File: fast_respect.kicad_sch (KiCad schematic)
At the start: 16 parts, among them J1_1 Conn_02x04_Odd_Even, SW1_1 SW_Push, SW1_2 SW_Push, U1_1 STM32F446RETx

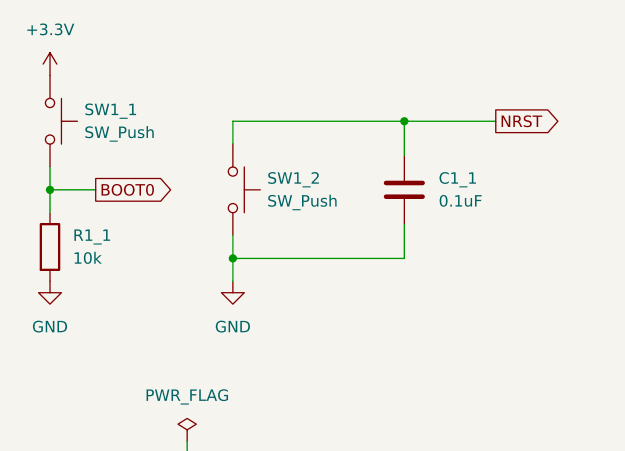
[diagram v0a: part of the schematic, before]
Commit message: 一部のスイッチの名称変更
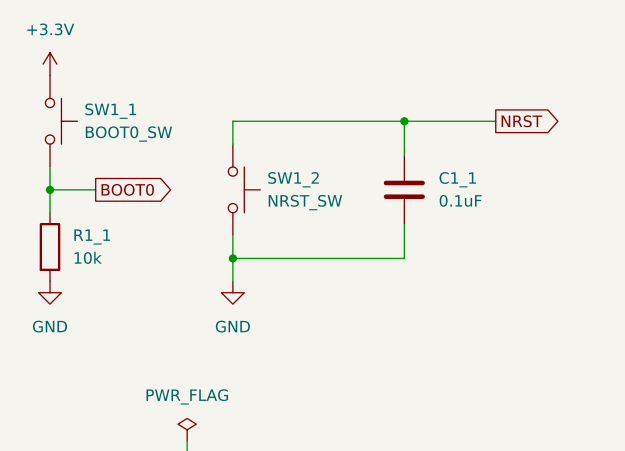
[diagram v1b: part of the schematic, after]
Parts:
- SW1_1: value SW_Push -> BOOT0_SW
- SW1_2: value SW_Push -> NRST_SW
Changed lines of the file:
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@@
       (effects (font (size 1.27 1.27)) (justify left))
     )
-    (property "Value" "SW_Push" (at 49.53 41.91 90)
+    (property "Value" "NRST_SW" (at 49.53 41.91 90)
       (effects (font (size 1.27 1.27)) (justify left))
     )
@@
       (effects (font (size 1.27 1.27)) (justify left))
     )
-    (property "Value" "SW_Push" (at 29.21 34.29 90)
+    (property "Value" "BOOT0_SW" (at 29.21 34.29 90)
       (effects (font (size 1.27 1.27)) (justify left))
     )

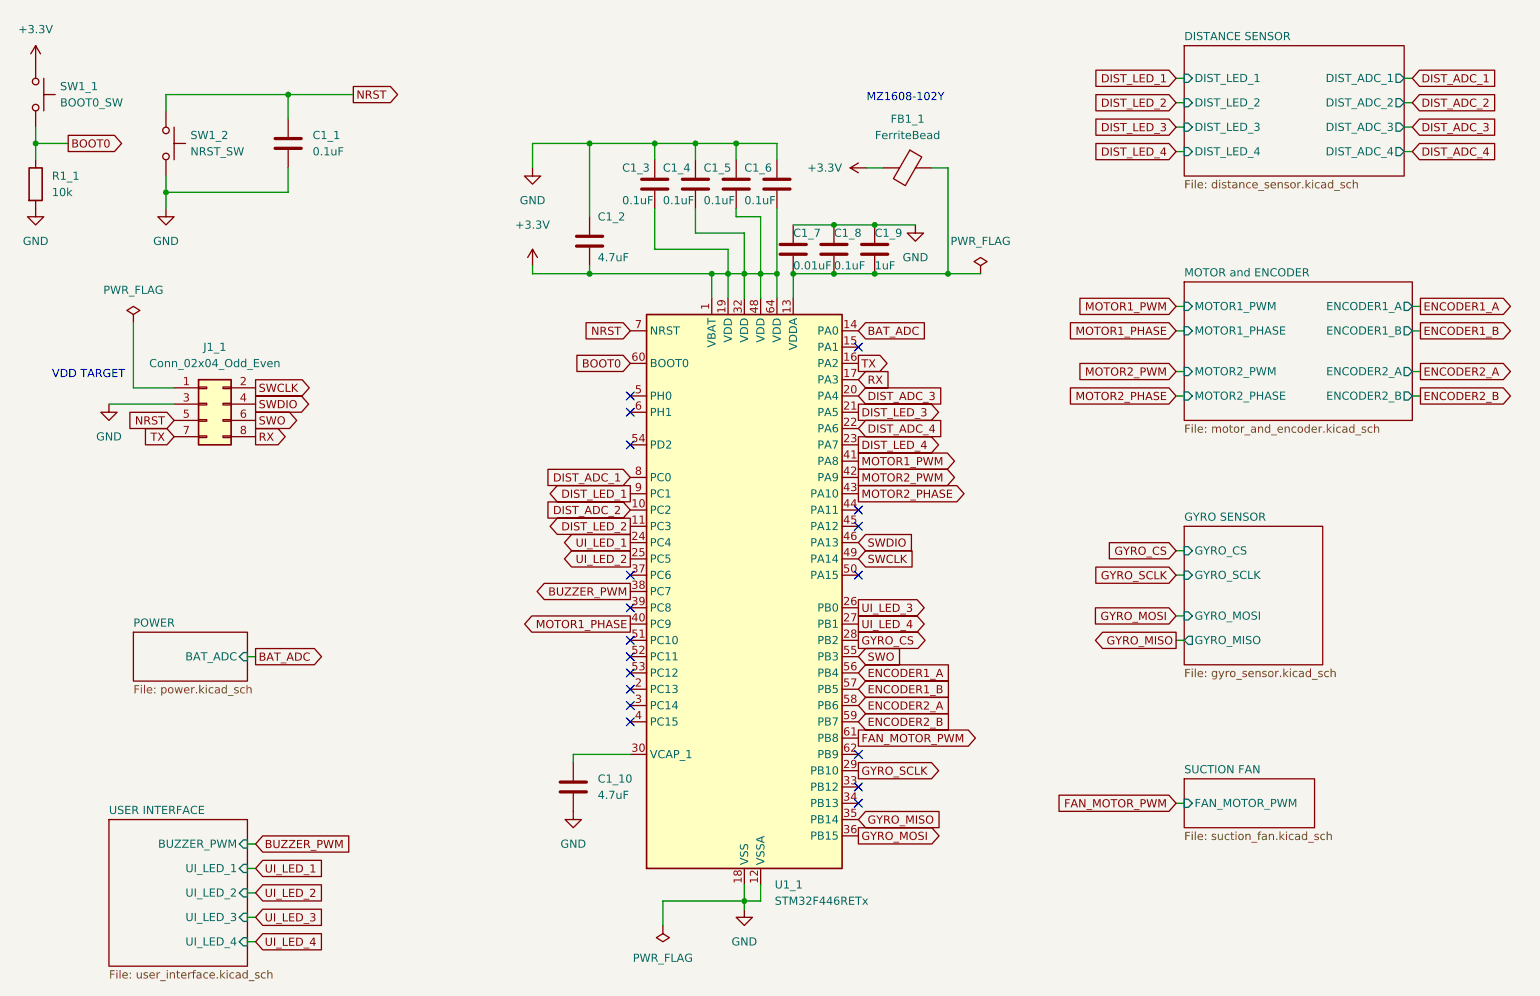
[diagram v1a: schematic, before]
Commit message: UIスイッチ３種類をマイコンピンに割り当て忘れてたので割り当てた
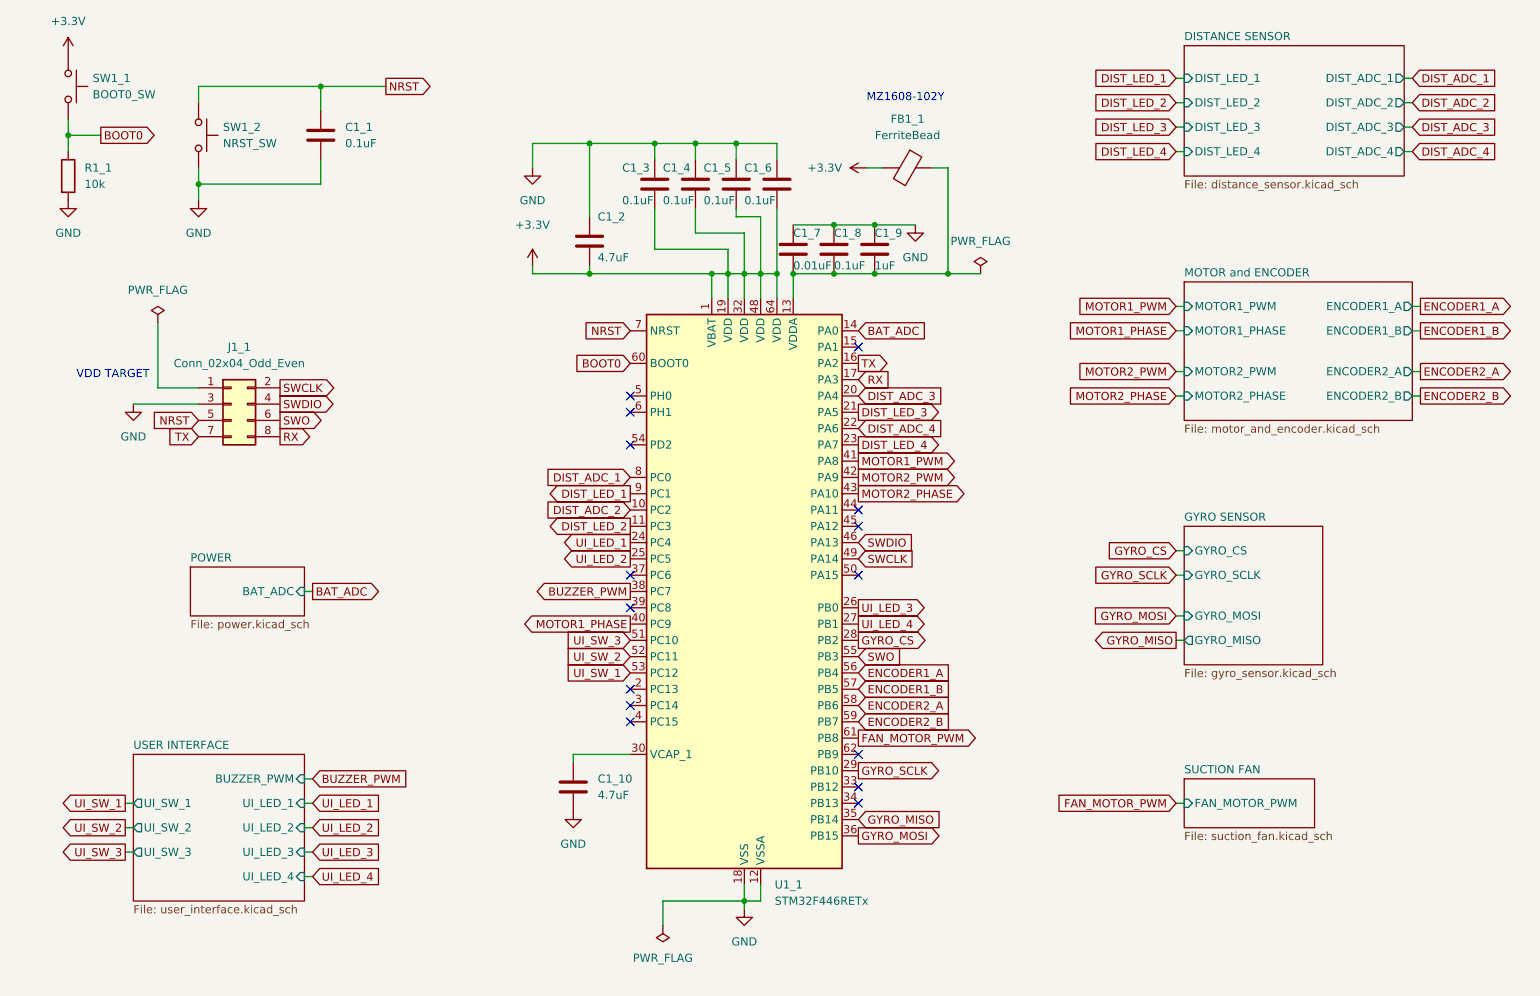
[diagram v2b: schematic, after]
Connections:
- net UI_SW_3: now reaches U1_1.51 (PC10)
- net UI_SW_2: now reaches U1_1.52 (PC11)
- net UI_SW_1: now reaches U1_1.53 (PC12)
- no-connect marks 18 -> 15
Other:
- sheet USER INTERFACE ports: added UI_SW_1, UI_SW_2, UI_SW_3; removed none
- moved on the sheet: C1_1, J1_1, R1_1, SW1_1, SW1_2

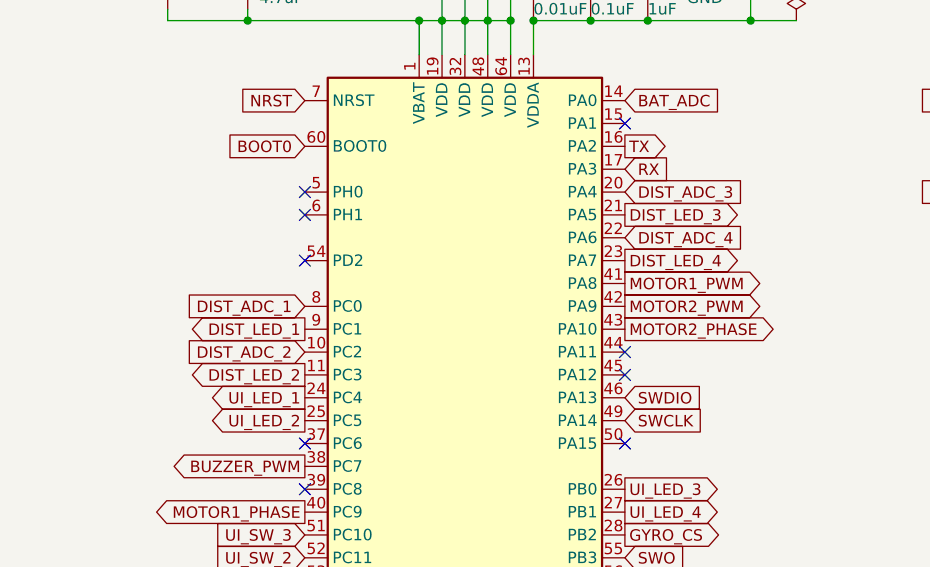
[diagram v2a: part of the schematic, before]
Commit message: 距離センサのPCB位置を考慮してピン割り当てを変更した（1,2,3,4 -> 4,3,2,1）
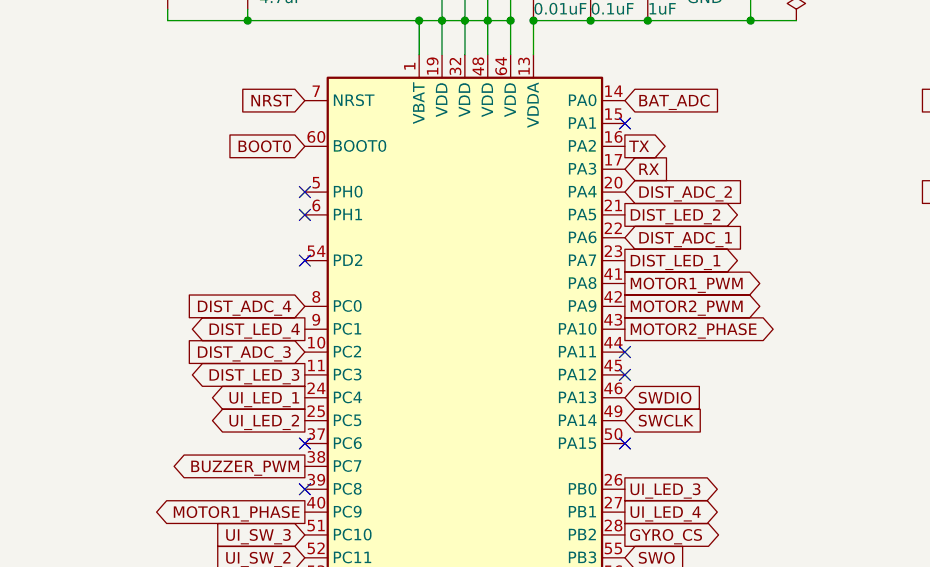
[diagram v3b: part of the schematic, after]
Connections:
- net DIST_ADC_1: now also U1_1.22 (PA6); no longer U1_1.8 (PC0)
- net DIST_ADC_2: now also U1_1.20 (PA4); no longer U1_1.10 (PC2)
- net DIST_ADC_3: now also U1_1.10 (PC2); no longer U1_1.20 (PA4)
- net DIST_ADC_4: now also U1_1.8 (PC0); no longer U1_1.22 (PA6)
- net DIST_LED_1: now also U1_1.23 (PA7); no longer U1_1.9 (PC1)
- net DIST_LED_2: now also U1_1.21 (PA5); no longer U1_1.11 (PC3)
- net DIST_LED_3: now also U1_1.11 (PC3); no longer U1_1.21 (PA5)
- net DIST_LED_4: now also U1_1.9 (PC1); no longer U1_1.23 (PA7)
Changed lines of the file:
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@@
     )
   )
-  (global_label "DIST_LED_4" (shape output) (at 153.67 87.63 0) (fields_autoplaced)
+  (global_label "DIST_LED_1" (shape output) (at 153.67 87.63 0) (fields_autoplaced)
     (effects (font (size 1.27 1.27)) (justify left))
     (property "Intersheetrefs" "${INTERSHEET_REFS}" (at 167.2989 87.63 0)
@@
     )
   )
-  (global_label "DIST_ADC_2" (shape input) (at 118.11 97.79 180) (fields_autoplaced)
+  (global_label "DIST_ADC_3" (shape input) (at 118.11 97.79 180) (fields_autoplaced)
     (effects (font (size 1.27 1.27)) (justify right))
     (property "Intersheetrefs" "${INTERSHEET_REFS}" (at 104.2996 97.79 0)
@@
     )
   )
-  (global_label "DIST_ADC_4" (shape input) (at 153.67 85.09 0) (fields_autoplaced)
+  (global_label "DIST_ADC_1" (shape input) (at 153.67 85.09 0) (fields_autoplaced)
     (effects (font (size 1.27 1.27)) (justify left))
     (property "Intersheetrefs" "${INTERSHEET_REFS}" (at 167.4804 85.09 0)
@@
     )
   )
-  (global_label "DIST_LED_2" (shape output) (at 118.11 100.33 180) (fields_autoplaced)
+  (global_label "DIST_LED_3" (shape output) (at 118.11 100.33 180) (fields_autoplaced)
     (effects (font (size 1.27 1.27)) (justify right))
     (property "Intersheetrefs" "${INTERSHEET_REFS}" (at 104.4811 100.33 0)
@@
     )
   )
-  (global_label "DIST_LED_3" (shape output) (at 153.67 82.55 0) (fields_autoplaced)
+  (global_label "DIST_LED_2" (shape output) (at 153.67 82.55 0) (fields_autoplaced)
     (effects (font (size 1.27 1.27)) (justify left))
     (property "Intersheetrefs" "${INTERSHEET_REFS}" (at 167.2989 82.55 0)
@@
     )
   )
-  (global_label "DIST_ADC_3" (shape input) (at 153.67 80.01 0) (fields_autoplaced)
+  (global_label "DIST_ADC_2" (shape input) (at 153.67 80.01 0) (fields_autoplaced)
     (effects (font (size 1.27 1.27)) (justify left))
     (property "Intersheetrefs" "${INTERSHEET_REFS}" (at 167.4804 80.01 0)
@@
     )
   )
-  (global_label "DIST_LED_1" (shape output) (at 118.11 95.25 180) (fields_autoplaced)
+  (global_label "DIST_LED_4" (shape output) (at 118.11 95.25 180) (fields_autoplaced)
     (effects (font (size 1.27 1.27)) (justify right))
     (property "Intersheetrefs" "${INTERSHEET_REFS}" (at 104.4811 95.25 0)
@@
     )
   )
-  (global_label "DIST_ADC_1" (shape input) (at 118.11 92.71 180) (fields_autoplaced)
+  (global_label "DIST_ADC_4" (shape input) (at 118.11 92.71 180) (fields_autoplaced)
     (effects (font (size 1.27 1.27)) (justify right))
     (property "Intersheetrefs" "${INTERSHEET_REFS}" (at 104.2996 92.71 0)
